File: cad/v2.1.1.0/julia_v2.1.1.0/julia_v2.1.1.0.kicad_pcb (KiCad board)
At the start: 4 copper layers, 63.2 x 47.8 mm, 104 parts, among them J1 Barrel_Jack_Switch, J2 JTAG/C2/UART Header, J4 Molex 0541044031, J5 Molex 0522710679, U1 EP4CE6F17, U2 AZ1117-3.3, U3 AZ1117-2.5, U4 NCP565ST12T3G, U5 W25Q80DVSNIG, U6 EFM8BB21F16I-C-QFN20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

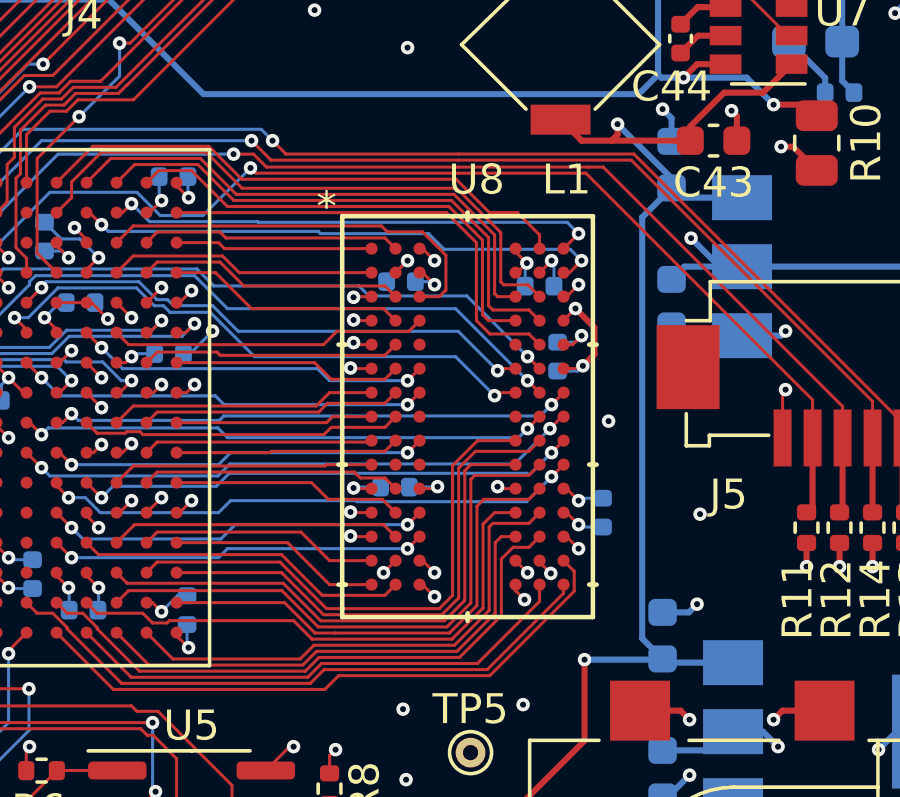
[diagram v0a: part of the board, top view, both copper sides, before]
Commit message: Several more 3d models
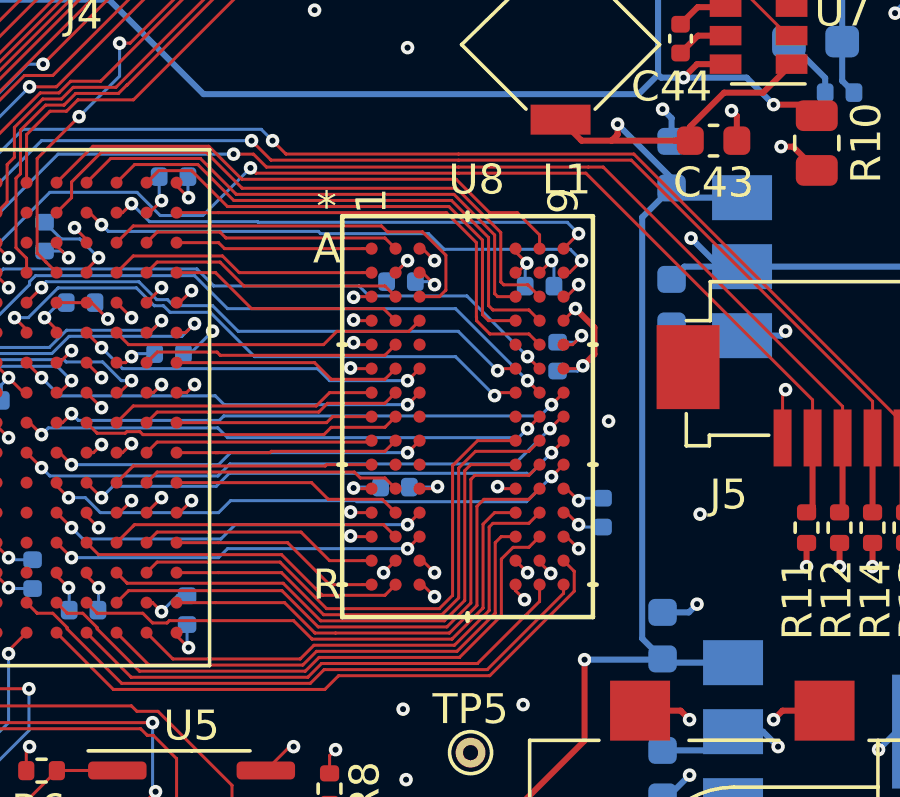
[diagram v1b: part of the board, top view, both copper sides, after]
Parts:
- U6: footprint Package_DFN_QFN:SiliconLabs_QFN-20-1EP_3x3mm_P0.5mm_EP1.8x1.8mm -> ik:SiliconLabs_QFN-20-1EP_3x3mm_P0.5mm_EP1.8x1.8mm

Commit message: Updated 3d rendering
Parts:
- H1, H2, H3, H4: footprint MountingHole:MountingHole_2.2mm_M2_Pad -> ik:MountingHole_2.2mm_M2_Pad
- X1: footprint Oscillator:Oscillator_SMD_EuroQuartz_XO91-4Pin_7.0x5.0mm -> ik:Oscillator_SMD_EuroQuartz_XO91-4Pin_7.0x5.0mm
